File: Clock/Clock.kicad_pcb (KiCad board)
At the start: 2 copper layers, 99.6 x 59.9 mm, 39 parts, among them J1 Conn_01x16, J2 Conn_01x16, SW1 SW_Push, SW2 SW_Push, SW3 SW_Push, SW4 SW_Push, U1 74LS76, U2 74LS76, U3 74LS08, U4 74LS08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

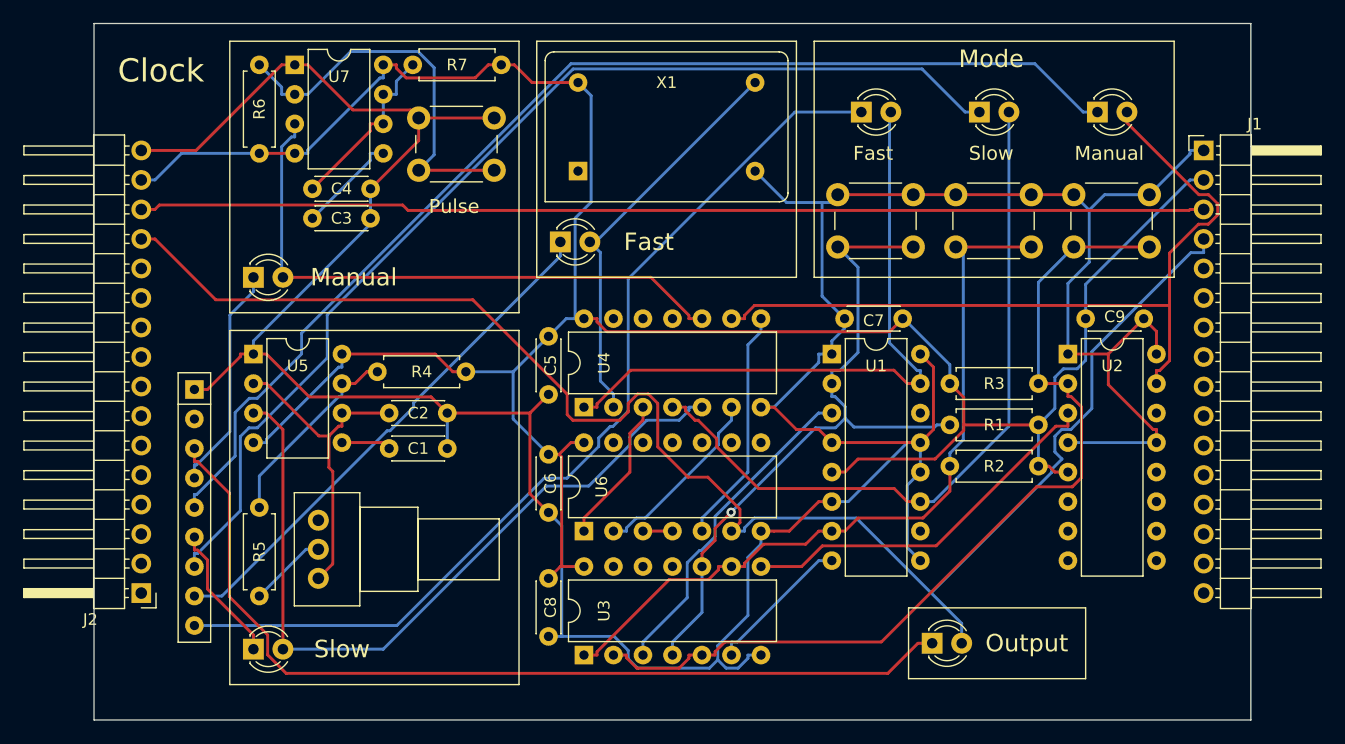
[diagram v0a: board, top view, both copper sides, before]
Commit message: Fixed floating inputs; improved power; added parts list; replaced JK latches
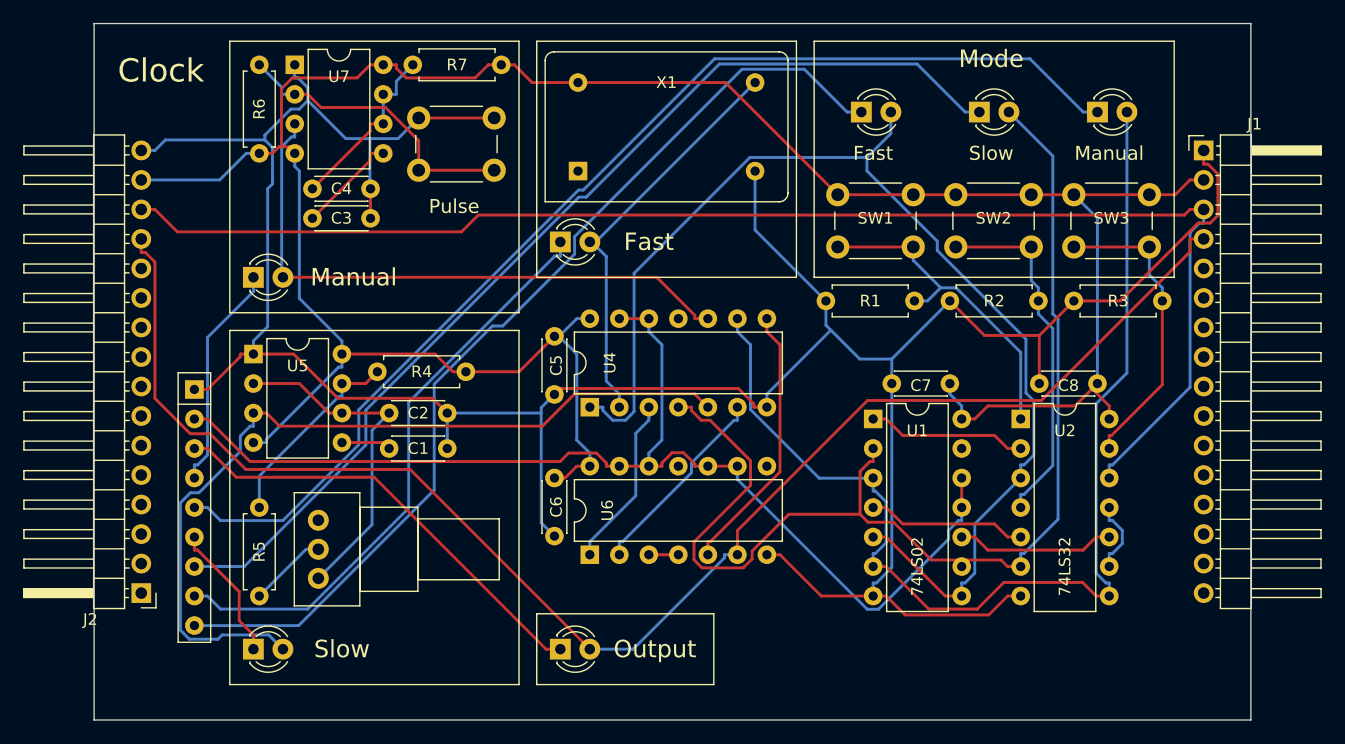
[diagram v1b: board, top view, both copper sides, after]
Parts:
- removed C9: 0.1uF, Capacitor_THT:C_Disc_D4.3mm_W1.9mm_P5.00mm
- removed U3: 74LS08, Package_DIP:DIP-14_W7.62mm
- U1: value 74LS76 -> 74LS02; footprint Package_DIP:DIP-16_W7.62mm -> Package_DIP:DIP-14_W7.62mm
- U2: value 74LS76 -> 74LS32; footprint Package_DIP:DIP-16_W7.62mm -> Package_DIP:DIP-14_W7.62mm
- moved C8 50.1 mm to (117.9, 65.0), turned to 180 degrees
- moved D7 32.0 mm to (71.6, 87.9)
- moved R1 21.2 mm to (94.5, 57.9), turned to 0 degrees
- moved R2 16.1 mm to (105.2, 57.9), turned to 0 degrees
- moved R3 12.8 mm to (115.8, 57.9)
- moved C7 6.91 mm to (105.2, 65.0)
- moved U2 6.91 mm to (111.3, 68.1)
- moved U1 6.62 mm to (98.6, 68.1)
- moved C6 2.09 mm to (71.1, 73.2)
- moved U6 2.09 mm to (74.2, 79.8)
- moved C5 0.51 mm to (71.1, 61.0)
- moved U4 0.51 mm to (74.2, 67.1)
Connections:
- R1 pad 1: VCC -> GND
- R2 pad 1: VCC -> GND
- R3 pad 1: VCC -> GND
- RN1 pad 2: Net-(RN1-Pad2) -> GND_1k
- SW1 pad 1: GND -> VCC
- SW2 pad 1: GND -> VCC
- SW3 pad 1: GND -> VCC
- U1 pad 1: GND -> Net-(U1-Pad1)
- U1 pad 11: Net-(D3-Pad2) -> GND_1k
- U1 pad 12: GND -> GND_1k
- U1 pad 13: GND -> Net-(U1-Pad13)
- U1 pad 14: Net-(U1-Pad14) -> VCC
- U1 pad 2: Net-(R1-Pad2) -> Net-(D3-Pad2)
- U1 pad 3: Net-(U1-Pad3) -> Net-(D5-Pad2)
- U1 pad 4: GND -> Net-(U1-Pad4)
- U1 pad 5: VCC -> Net-(D1-Pad2)
- U1 pad 6: GND -> Net-(D5-Pad2)
- U1 pad 7: Net-(R2-Pad2) -> GND
- U1 pad 8: Net-(U1-Pad8) -> Net-(D1-Pad2)
- U1 pad 9: GND -> Net-(D3-Pad2)
- U2 pad 1: GND -> Net-(R1-Pad2)
- U2 pad 10: (no net) -> Net-(U1-Pad10)
- U2 pad 11: (no net) -> Net-(U2-Pad11)
- U2 pad 12: (no net) -> RESET
- U2 pad 13: GND -> Net-(R3-Pad2)
- U2 pad 14: Net-(U2-Pad14) -> VCC
- U2 pad 2: Net-(R3-Pad2) -> Net-(U1-Pad1)
- U2 pad 3: Net-(U2-Pad3) -> Net-(D1-Pad2)
- U2 pad 4: GND -> Net-(R2-Pad2)
- U2 pad 5: VCC -> Net-(U1-Pad4)
- U2 pad 6: (no net) -> Net-(D3-Pad2)
- U2 pad 7: (no net) -> GND
- U2 pad 8: (no net) -> Net-(D5-Pad2)
- U2 pad 9: (no net) -> Net-(U2-Pad11)
- U4 pad 11: (no net) -> Net-(U4-Pad11)
- U4 pad 12: (no net) -> GND_1k
- U4 pad 13: (no net) -> GND_1k
- U6 pad 10: (no net) -> GND_1k
- U6 pad 11: (no net) -> Net-(U6-Pad11)
- U6 pad 12: (no net) -> GND_1k
- U6 pad 13: (no net) -> GND_1k
- U6 pad 8: (no net) -> Net-(U6-Pad8)
- U6 pad 9: (no net) -> GND_1k
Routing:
- net GND_1k: track 0.00 -> 98.9 mm
- net GND: track 311.9 -> 256.9 mm
- net Net-(R3-Pad2): track 78.8 -> 26.3 mm
- net Net-(D1-Pad2): track 55.6 -> 101.9 mm
- net Net-(D7-Pad1): track 79.5 -> 38.7 mm
- net Net-(D3-Pad2): track 62.6 -> 100.6 mm
- net Net-(R2-Pad2): track 66.1 -> 31.0 mm
- net Net-(U2-Pad3): track 32.5 -> 0.00 mm
- net Net-(R1-Pad2): track 60.9 -> 28.6 mm, vias 1 -> 0
- net Net-(D5-Pad2): track 68.3 -> 96.7 mm
- net Net-(U1-Pad3): track 28.3 -> 0.00 mm
- net RESET: track 91.8 -> 119.9 mm
- net Net-(U1-Pad4): track 0.00 -> 13.8 mm
- net Net-(U1-Pad1): track 0.00 -> 13.8 mm
- net Net-(U1-Pad10): track 0.00 -> 13.6 mm
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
